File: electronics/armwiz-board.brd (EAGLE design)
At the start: 99.1 x 51.5 mm, 135 parts, among them IC1 STM32F_48PIN, IC2 TXS0108, IC3 TLV70033DCK, J1 MICRO-SDCARD-CONNECTOR-330006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, J15 Cortex Debug, J16 ST-Link v2, J2 CORTEX_DEBUGSMD, Q1 IRLML5103, U1 STM32F10XRXT6, U4 MIC5219-3.3V, X1 FH12-12S-1S, Y1 8MHz, Y3 32.768kHz

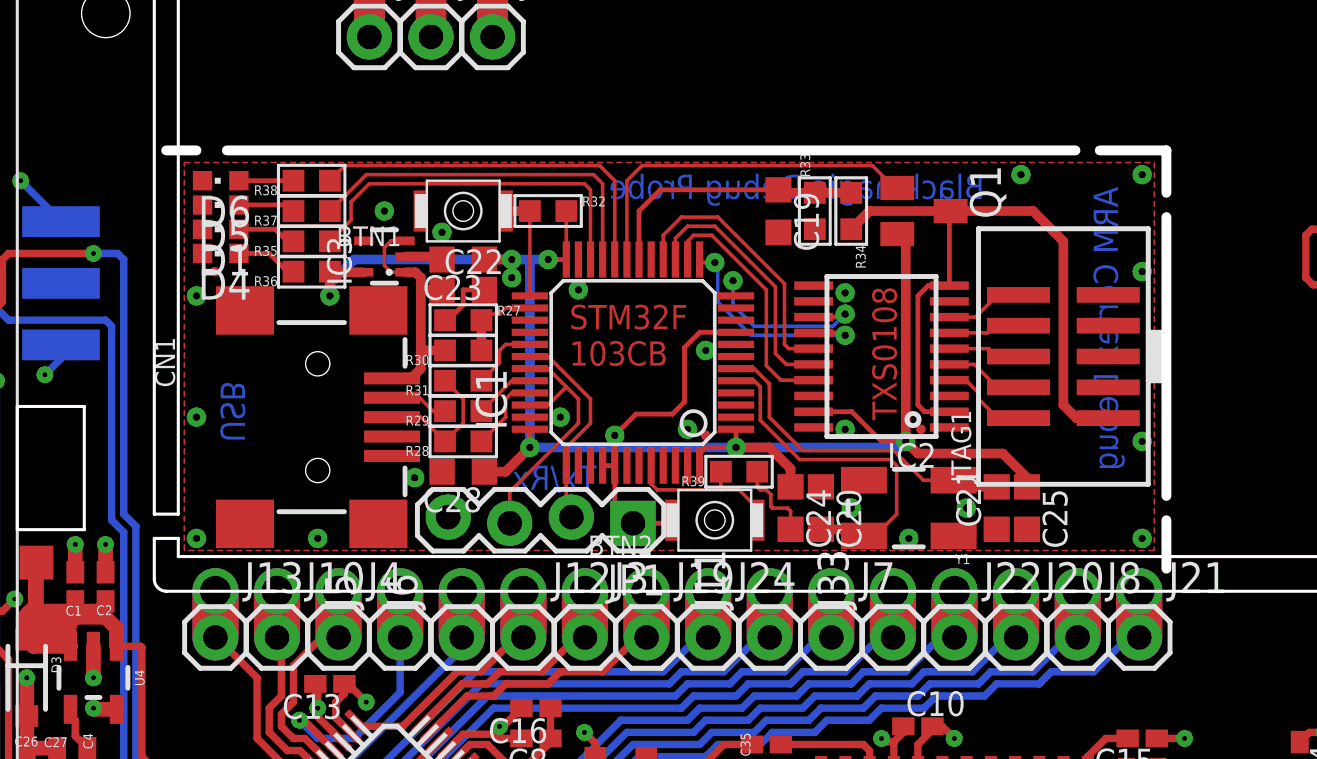
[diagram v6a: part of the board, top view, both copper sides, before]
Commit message: Removed Black Magic probe from design file.
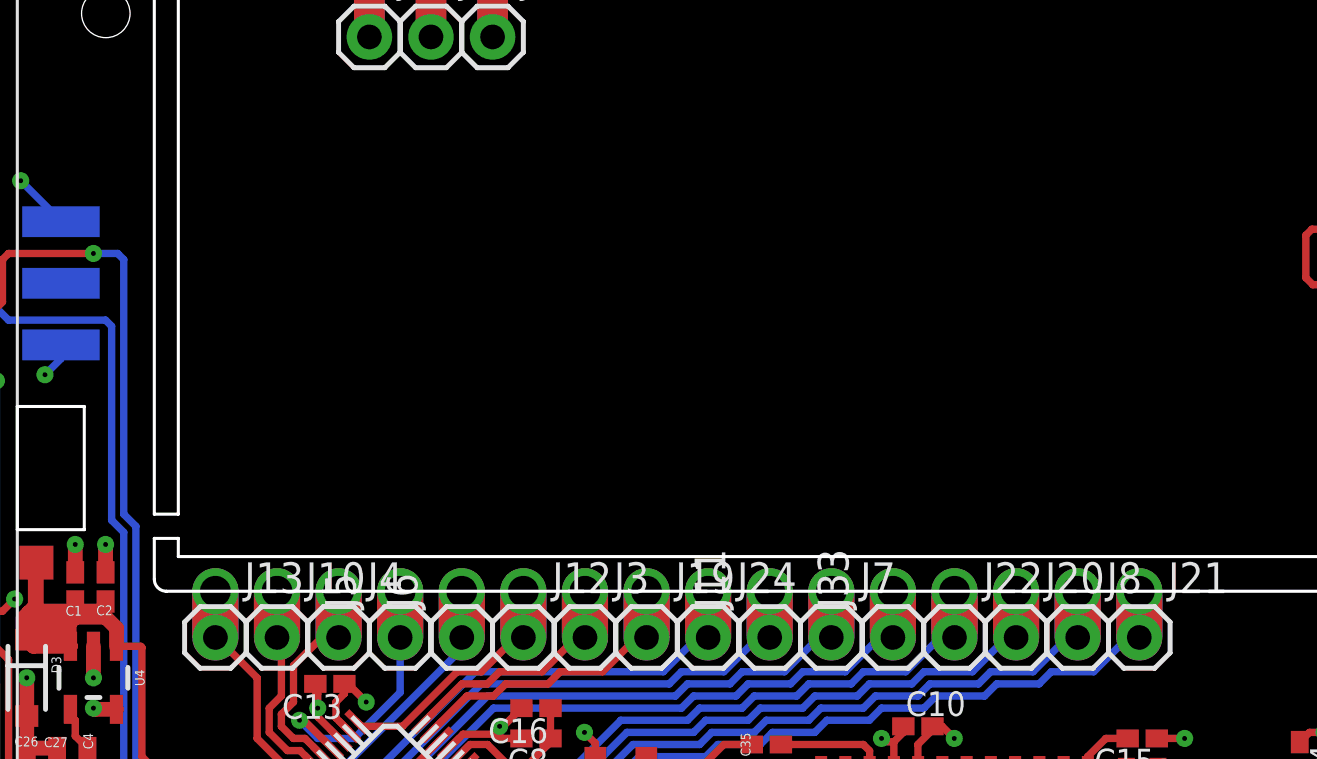
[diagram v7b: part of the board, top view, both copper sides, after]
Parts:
- removed BTN1, BTN2: SPST.B3U-1000P(M)-B, omron:B3U-1000P(M)-B
- removed C19, C24, C25, C28: 100nF, resistor:C0603K
- removed C20, C21: 18pF, resistor:C0603K
- removed C22, C23: 1µF, resistor:C0603K
- removed CN1: (no value), microbuilder_v3:USB-MINIB
- removed D1: RED, led:CHIPLED_0603
- removed D4: GREEN, led:CHIPLED_0603
- removed D5, D6: YELLOW, led:CHIPLED_0603
- removed IC1: STM32F_48PIN, stm32f:TQFP48
- removed IC2: TXS0108, dan-translate:TSSOP20
- removed IC3: TLV70033DCK, tlv700:SC70-5L
- removed JP1: (no value), SparkFun:1X04_LOCK
- removed JTAG1: (no value), microbuilder_v3:2X05_1.27MM_SMT
- removed Q1: IRLML5103, transistor-small-signal:SOT23
- removed R27, R32, R33, R39: 10K, microbuilder:0603-MINI
- removed R28, R29: 22Ω, microbuilder:0603-MINI
- removed R30, R34: 4K7, microbuilder:0603-MINI
- removed R31: 1K5, microbuilder:0603-MINI
- removed R35, R36, R37, R38: 390Ω, microbuilder:0603-MINI
- removed Y1: 8MHz, SparkFun:CRYSTAL-SMD-5X3
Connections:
- removed net 3.3V1: BTN2.2, C23.1, C24.1, C25.1, C28.1, IC1.1, IC1.24, IC1.36, IC1.40, IC1.41, IC1.48, IC1.9, IC2.19, IC3.5, JP1.1, Q1.2, R32.2, R36.1
- removed net 5.0V: C22.1, CN1.VBUS, IC3.1, IC3.3, R30.2
- removed net BOOT2: BTN2.1, IC1.44, R39.2
- removed net D+1: CN1.D+, R28.2, R31.2
- removed net D-1: CN1.D-, R29.2
- removed net FORCE_BOOTLOADER: BTN1.1, IC1.25, R32.1
- removed net GND1: BTN1.2, C19.2, C20.1, C21.1, C22.2, C23.2, C24.2, C25.2, C28.2, CN1.GND, CN1.ID, D1.C, D4.C, D5.C, D6.C, IC1.23, IC1.35, IC1.47, IC1.8, IC2.11, IC2.12, IC2.18, IC2.20, IC3.2, JP1.4, JTAG1.3, JTAG1.5, JTAG1.9, R27.1, R33.1, R39.1
- removed net LED0: IC1.20, R38.1
- removed net LED1: IC1.21, R37.1
- removed net LED2: IC1.22, R35.1
- removed net LPC_XTAL2: C21.2, IC1.6, Y1.1
- removed net N$10: D1.A, R35.2
- removed net N$17: D4.A, R36.2
- removed net N$25: D5.A, R37.2
- removed net N$26: D6.A, R38.2
- removed net OSC_IN1: C20.2, IC1.5, Y1.3
- removed net PWR_BR: IC1.19, Q1.1
- removed net RST: IC1.12, IC2.13
- removed net RXD: IC1.31, IC1.34, JP1.3
- removed net TARGET_POWER_ADC: C19.1, IC1.18, R33.2, R34.1
- removed net TARGET_RST: IC2.8, JTAG1.10
- removed net TARGET_TCK: IC2.5, JTAG1.4
- removed net TARGET_TDI: IC2.7, JTAG1.8
- removed net TARGET_TDO: IC2.6, JTAG1.6
- removed net TARGET_TMS: IC2.4, JTAG1.2
- removed net TCK: IC1.15, IC2.16
- removed net TDI: IC1.13, IC2.14
- removed net TDO: IC1.16, IC2.15
- removed net TMS: IC1.14, IC2.17
- removed net TPWR: IC2.10, IC2.2, JTAG1.1, Q1.3, R34.2
- removed net TXD: IC1.30, IC1.37, JP1.2
- removed net USB_DM: IC1.32, R29.1
- removed net USB_DP: IC1.33, R28.1
- removed net USB_ENUMERATE: IC1.29, R31.1
- removed net VBUS1: IC1.26, R27.2, R30.1
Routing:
- net 3.3V1: track 82.6 -> 0.00 mm, vias 7 -> 0
- net TPWR: track 28.9 -> 0.00 mm
- net LED0: track 15.5 -> 0.00 mm
- net LED2: track 15.2 -> 0.00 mm
- net LED1: track 15.2 -> 0.00 mm
- net PWR_BR: track 15.0 -> 0.00 mm
- net OSC_IN1: track 14.5 -> 0.00 mm
- net LPC_XTAL2: track 13.6 -> 0.00 mm
- net TDO: track 11.2 -> 0.00 mm
- net TARGET_POWER_ADC: track 11.2 -> 0.00 mm
- net TCK: track 10.8 -> 0.00 mm
- net RXD: track 10.6 -> 0.00 mm
- net 5.0V: track 10.4 -> 0.00 mm
- net TMS: track 10.4 -> 0.00 mm
- net TDI: track 9.51 -> 0.00 mm, vias 2 -> 0
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- removed copper zone on layer 1, net GND1
- removed copper zone on layer 16, net GND1
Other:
- outline, holes or cut-outs redrawn
- board text removed: "ARM Cortex Debug"
- board text removed: "Blackmagic Debug Probe"
- board text removed: "STM32F 103CB"
- board text removed: "TXS0108"
- board text removed: "Tx/Rx"
- board text removed: "USB"

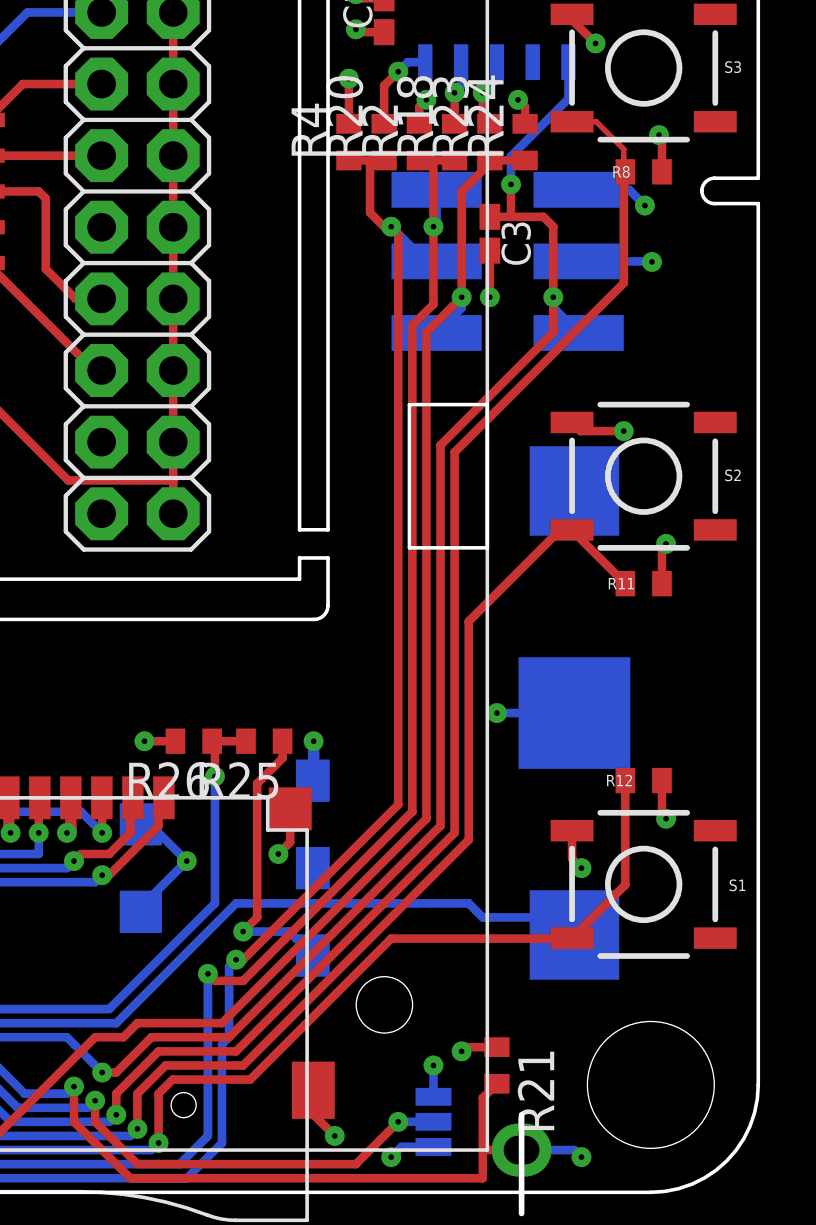
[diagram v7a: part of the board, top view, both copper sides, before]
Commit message: Fixed an issue. Traces were going through the LCD cutout.
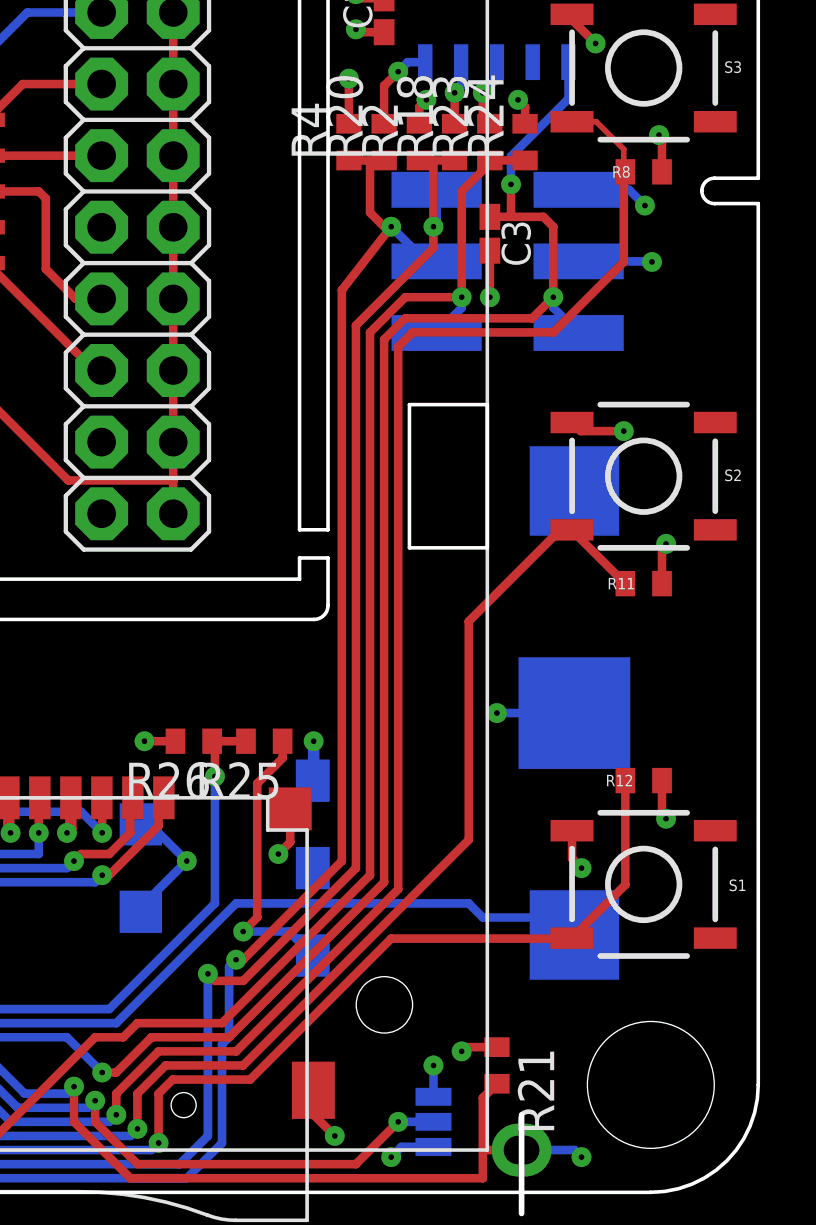
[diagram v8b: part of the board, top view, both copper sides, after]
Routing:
- net SW_A: track 103.1 -> 106.1 mm
- net NRST: track 102.2 -> 104.8 mm
- net SWO: track 91.6 -> 92.8 mm
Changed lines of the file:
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@@
 <layer number="37" name="tTest" color="7" fill="1" visible="no" active="yes"/>
 <layer number="38" name="bTest" color="7" fill="1" visible="no" active="yes"/>
-<layer number="39" name="tKeepout" color="4" fill="11" visible="yes" active="yes"/>
-<layer number="40" name="bKeepout" color="1" fill="11" visible="yes" active="yes"/>
-<layer number="41" name="tRestrict" color="4" fill="10" visible="yes" active="yes"/>
-<layer number="42" name="bRestrict" color="1" fill="10" visible="yes" active="yes"/>
+<layer number="39" name="tKeepout" color="4" fill="11" visible="no" active="yes"/>
+<layer number="40" name="bKeepout" color="1" fill="11" visible="no" active="yes"/>
+<layer number="41" name="tRestrict" color="4" fill="10" visible="no" active="yes"/>
+<layer number="42" name="bRestrict" color="1" fill="10" visible="no" active="yes"/>
 <layer number="43" name="vRestrict" color="2" fill="10" visible="no" active="yes"/>
 <layer number="44" name="Drills" color="7" fill="1" visible="no" active="yes"/>
@@
 <wire x1="73.75" y1="3.5" x2="75.25" y2="5" width="0.3048" layer="1"/>
 <wire x1="75.25" y1="5" x2="78" y2="5" width="0.3048" layer="1"/>
-<wire x1="78" y1="5" x2="85.75" y2="12.75" width="0.3048" layer="1"/>
-<wire x1="91.75" y1="32.25" x2="91.75" y2="36.139" width="0.3048" layer="1"/>
+<wire x1="78" y1="5" x2="83.75" y2="10.75" width="0.3048" layer="1"/>
+<wire x1="91.75" y1="33" x2="91.75" y2="36.139" width="0.3048" layer="1"/>
 <wire x1="91.75" y1="36.139" x2="91.806" y2="36.195" width="0.3048" layer="1"/>
-<wire x1="85.75" y1="12.75" x2="85.75" y2="26.25" width="0.3048" layer="1"/>
-<wire x1="85.75" y1="26.25" x2="91.75" y2="32.25" width="0.3048" layer="1"/>
+<wire x1="83.75" y1="10.75" x2="83.75" y2="30" width="0.3048" layer="1"/>
 <wire x1="27.25" y1="4.75" x2="26.75" y2="4.75" width="0.3048" layer="16"/>
 <wire x1="26.75" y1="4.75" x2="26" y2="5.5" width="0.3048" layer="16"/>
 <wire x1="26" y1="5.5" x2="26" y2="6" width="0.3048" layer="16"/>
 <wire x1="26" y1="6" x2="25.5" y2="6.5" width="0.3048" layer="16"/>
+<wire x1="83.75" y1="30" x2="84.25" y2="30.5" width="0.3048" layer="1"/>
+<wire x1="84.25" y1="30.5" x2="89.25" y2="30.5" width="0.3048" layer="1"/>
+<wire x1="89.25" y1="30.5" x2="91.75" y2="33" width="0.3048" layer="1"/>
 </signal>
 <signal name="USB_VCC">
@@
 <wire x1="73.75" y1="4.25" x2="75" y2="5.5" width="0.3048" layer="1"/>
 <wire x1="75" y1="5.5" x2="77.75" y2="5.5" width="0.3048" layer="1"/>
-<wire x1="77.75" y1="5.5" x2="85.25" y2="13" width="0.3048" layer="1"/>
-<wire x1="85.25" y1="13" x2="85.25" y2="26.5" width="0.3048" layer="1"/>
-<wire x1="85.25" y1="26.5" x2="89.25" y2="30.5" width="0.3048" layer="1"/>
-<wire x1="89.25" y1="30.5" x2="89.25" y2="31.75" width="0.3048" layer="1"/>
+<wire x1="77.75" y1="5.5" x2="83.25" y2="11" width="0.3048" layer="1"/>
+<wire x1="83.25" y1="11" x2="83.25" y2="30.25" width="0.3048" layer="1"/>
 <wire x1="29.25" y1="5" x2="27.25" y2="7" width="0.3048" layer="16"/>
 <wire x1="27.25" y1="7" x2="27.25" y2="8.5" width="0.3048" layer="1"/>
 <wire x1="27.25" y1="8.5" x2="29" y2="10.25" width="0.3048" layer="1"/>
 <wire x1="29" y1="10.25" x2="29" y2="11.189340625" width="0.3048" layer="1"/>
+<wire x1="83.25" y1="30.25" x2="84" y2="31" width="0.3048" layer="1"/>
+<wire x1="84" y1="31" x2="88.5" y2="31" width="0.3048" layer="1"/>
+<wire x1="88.5" y1="31" x2="89.25" y2="31.75" width="0.3048" layer="1"/>
 </signal>
 <signal name="OSC_IN">
@@
 <wire x1="77.25" y1="7.5" x2="78.25" y2="7.5" width="0.3048" layer="1"/>
 <wire x1="77" y1="2" x2="77" y2="7.75" width="0.3048" layer="16"/>
-<wire x1="78.25" y1="7.5" x2="84.25" y2="13.5" width="0.3048" layer="1"/>
-<wire x1="84.25" y1="13.5" x2="84.25" y2="30.75" width="0.3048" layer="1"/>
-<wire x1="84.25" y1="30.75" x2="85" y2="31.5" width="0.3048" layer="1"/>
-<wire x1="85" y1="31.5" x2="85" y2="34.25" width="0.3048" layer="1"/>
+<wire x1="78.25" y1="7.5" x2="82.25" y2="11.5" width="0.3048" layer="1"/>
+<wire x1="82.25" y1="11.5" x2="82.25" y2="30.75" width="0.3048" layer="1"/>
+<wire x1="82.25" y1="30.75" x2="85" y2="33.5" width="0.3048" layer="1"/>
+<wire x1="85" y1="33.5" x2="85" y2="34.25" width="0.3048" layer="1"/>
 <wire x1="27" y1="1" x2="26.25" y2="1.75" width="0.3048" layer="16"/>
 <wire x1="26.25" y1="1.75" x2="25.75" y2="1.75" width="0.3048" layer="16"/>
@@
 <wire x1="77.75" y1="8" x2="78" y2="8.25" width="0.3048" layer="16"/>
 <wire x1="78" y1="8.25" x2="78.25" y2="8.25" width="0.3048" layer="1"/>
-<wire x1="78.25" y1="8.25" x2="83.75" y2="13.75" width="0.3048" layer="1"/>
-<wire x1="83.75" y1="13.75" x2="83.75" y2="34" width="0.3048" layer="1"/>
-<wire x1="83.75" y1="34" x2="83.5" y2="34.25" width="0.3048" layer="1"/>
+<wire x1="78.25" y1="8.25" x2="81.75" y2="11.75" width="0.3048" layer="1"/>
+<wire x1="81.75" y1="11.75" x2="81.75" y2="32" width="0.3048" layer="1"/>
+<wire x1="81.75" y1="32" x2="83.5" y2="34.25" width="0.3048" layer="1"/>
 <wire x1="84.77" y1="33.02" x2="85.11" y2="33.02" width="0.3048" layer="16"/>
 <wire x1="24" y1="0.5" x2="22.75" y2="1.75" width="0.3048" layer="16"/>
@@
 <wire x1="74" y1="5.5" x2="74.5" y2="6" width="0.3048" layer="1"/>
 <wire x1="74.5" y1="6" x2="77.5" y2="6" width="0.3048" layer="1"/>
-<wire x1="77.5" y1="6" x2="84.75" y2="13.25" width="0.3048" layer="1"/>
-<wire x1="84.75" y1="13.25" x2="84.75" y2="30.5" width="0.3048" layer="1"/>
-<wire x1="84.75" y1="30.5" x2="86" y2="31.75" width="0.3048" layer="1"/>
+<wire x1="77.5" y1="6" x2="82.75" y2="11.25" width="0.3048" layer="1"/>
+<wire x1="82.75" y1="11.25" x2="82.75" y2="30.5" width="0.3048" layer="1"/>
+<wire x1="82.75" y1="30.5" x2="84" y2="31.75" width="0.3048" layer="1"/>
+<wire x1="84" y1="31.75" x2="86" y2="31.75" width="0.3048" layer="1"/>
 </signal>
 <signal name="N$5">
